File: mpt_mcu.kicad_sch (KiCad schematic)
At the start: 11 parts, among them SW2 KMR421GULCLFS, SW3 KMR421GULCLFS, U4 ESP32-S3-WROOM-1-N4R2

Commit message: Added Info-Table for STAT Pins and LEDS of Charger Work In Progress regulation for Display driving (currently not working)
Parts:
- R20: value 1k -> 100R; symbol db:resistor_0603/00.018.0009.0045 -> db:resistor_0603/00.018.0009.0044; Dist1# 311-1.00KHRCT-ND -> 311-100HRCT-ND; MFR# RC0603FR-071KL -> RC0603FR-07100RL
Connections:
- net +3V3 renamed +3V4
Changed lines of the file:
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@@
 			)
 		)
-		(property "Value" "+3V3"
+		(property "Value" "+3V4"
 			(at 88.9 46.6669 0)
 			(show_name no)
@@
 			)
 		)
-		(property "Value" "+3V3"
+		(property "Value" "+3V4"
 			(at 88.9 74.6069 0)
 			(show_name no)
@@
 			)
 		)
-		(property "Value" "+3V3"
+		(property "Value" "+3V4"
 			(at 209.55 56.8269 0)
 			(show_name no)
@@
 	)
 	(symbol
-		(lib_id "db:resistor_0603/00.018.0009.0045")
+		(lib_id "db:resistor_0603/00.018.0009.0044")
 		(at 209.55 66.04 0)
 		(unit 1)
@@
 			)
 		)
-		(property "Value" "1k"
+		(property "Value" "100R"
 			(at 211.074 67.2521 0)
 			(show_name no)
@@
 			)
 		)
-		(property "Description" "R 1k 0603"
+		(property "Description" "R 100R 0603"
 			(at 209.55 66.04 0)
 			(hide yes)
@@
 			)
 		)
-		(property "MFR#" "RC0603FR-071KL"
+		(property "MFR#" "RC0603FR-07100RL"
 			(at 209.55 66.04 0)
 			(hide yes)
@@
 			)
 		)
-		(property "Dist1#" "311-1.00KHRCT-ND"
+		(property "Dist1#" "311-100HRCT-ND"
 			(at 209.55 66.04 0)
 			(hide yes)
@@
 			)
 		)
-		(property "Value" "+3V3"
+		(property "Value" "+3V4"
 			(at 136.652 75.946 0)
 			(show_name no)

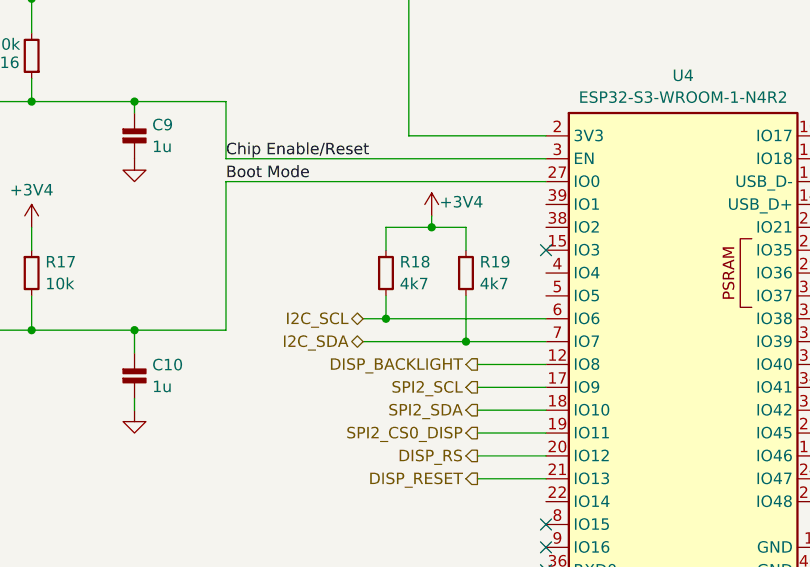
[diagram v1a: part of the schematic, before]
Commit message: Changed LED Driver for one with lower Headroom
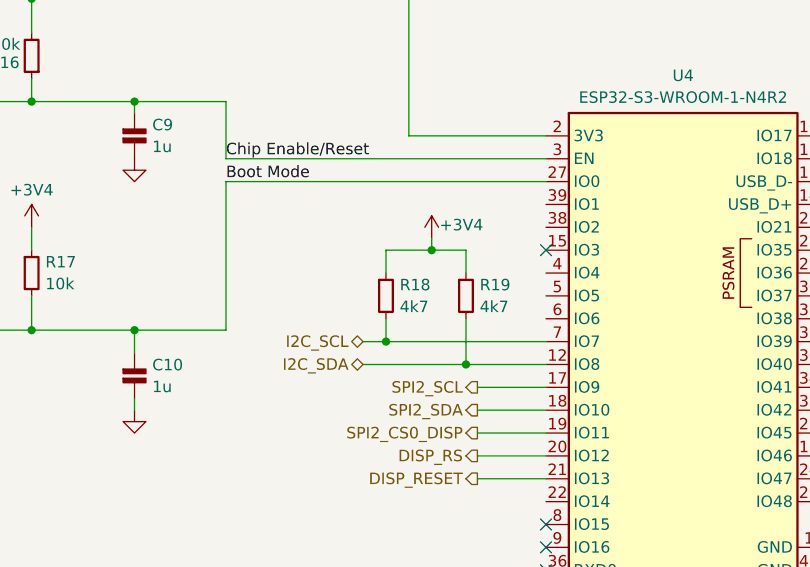
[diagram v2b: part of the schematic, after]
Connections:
- net DISP_BACKLIGHT is gone; now on net I2C_SDA: U4.12 (IO8)
- net I2C_SCL: now also U4.7 (IO7); no longer U4.6 (IO6)
- net I2C_SDA: no longer U4.7 (IO7)
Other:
- moved on the sheet: R18, R19

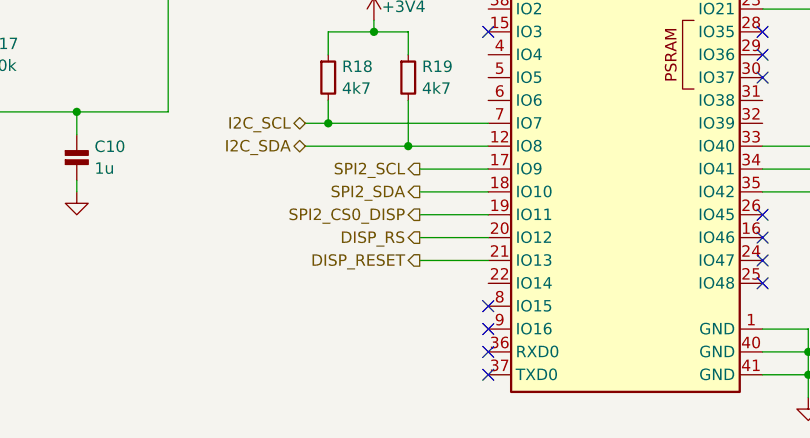
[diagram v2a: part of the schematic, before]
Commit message: RTC Finished, changes to User Buttons
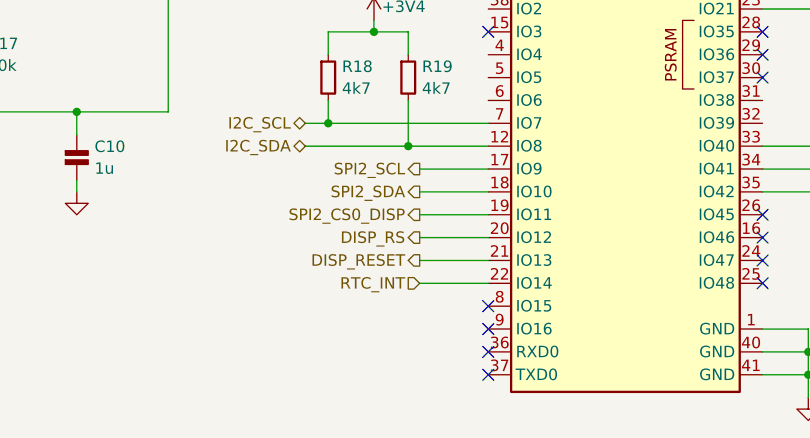
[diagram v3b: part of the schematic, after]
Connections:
- net RTC_INT: now reaches U4.22 (IO14)
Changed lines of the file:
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@@
+	(wire
+		(pts
+			(xy 138.43 109.22) (xy 146.05 109.22)
+		)
+		(stroke
+			(width 0)
+			(type default)
+		)
+	)
 	(wire
 		(pts
@@
 		(effects
 			(font
+				(size 1.27 1.27)
+			)
+			(justify right)
+		)
+	)
+	(hierarchical_label "RTC_INT"
+		(shape input)
+		(at 138.43 109.22 180)
+		(effects
+			(font

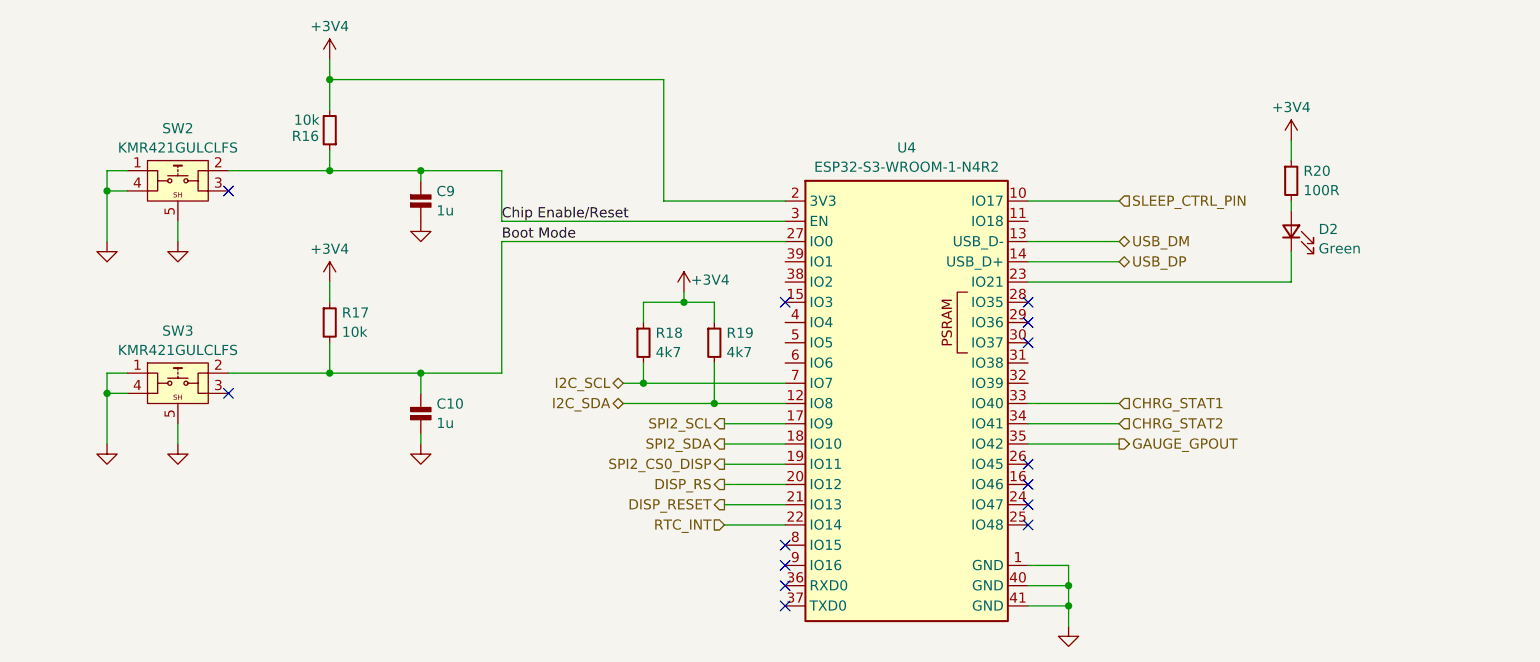
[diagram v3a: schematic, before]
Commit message: Updated PCB Layout with new Buck Boost, Display driver and STAT Led logic
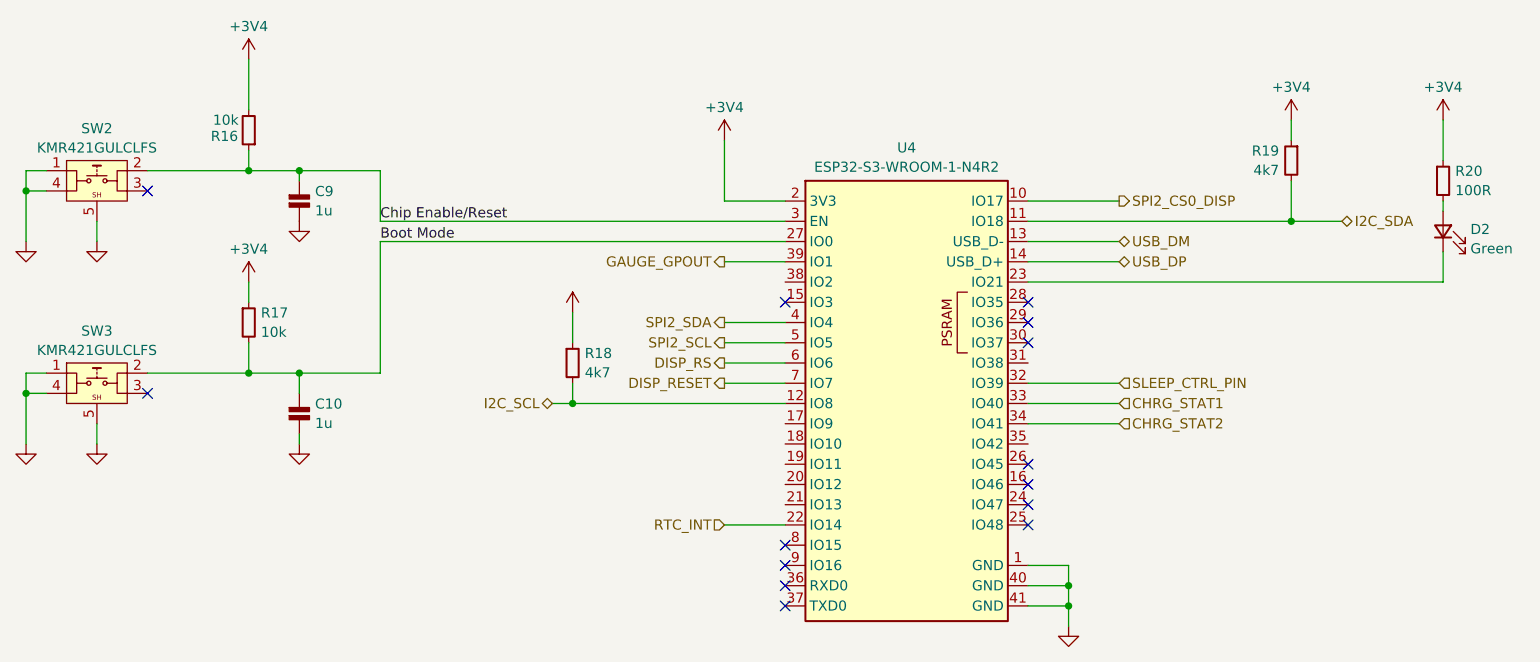
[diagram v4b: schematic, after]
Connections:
- net DISP_RESET: now also U4.7 (IO7); no longer U4.21 (IO13)
- net DISP_RS: now also U4.6 (IO6); no longer U4.20 (IO12)
- net GAUGE_GPOUT: now also U4.39 (IO1); no longer U4.35 (IO42)
- net I2C_SCL: now also U4.12 (IO8); no longer U4.7 (IO7)
- net I2C_SDA: now also U4.11 (IO18); no longer U4.12 (IO8)
- net SLEEP_CTRL_PIN: now also U4.32 (IO39); no longer U4.10 (IO17)
- net SPI2_CS0_DISP: now also U4.10 (IO17); no longer U4.19 (IO11)
- net SPI2_SCL: now also U4.5 (IO5); no longer U4.17 (IO9)
- net SPI2_SDA: now also U4.4 (IO4); no longer U4.18 (IO10)
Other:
- moved on the sheet: C10, C9, D2, R16, R17, R20, SW2, SW3

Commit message: Sleep Control Sub-Sheet created, Hirarchy Labels renamed connected
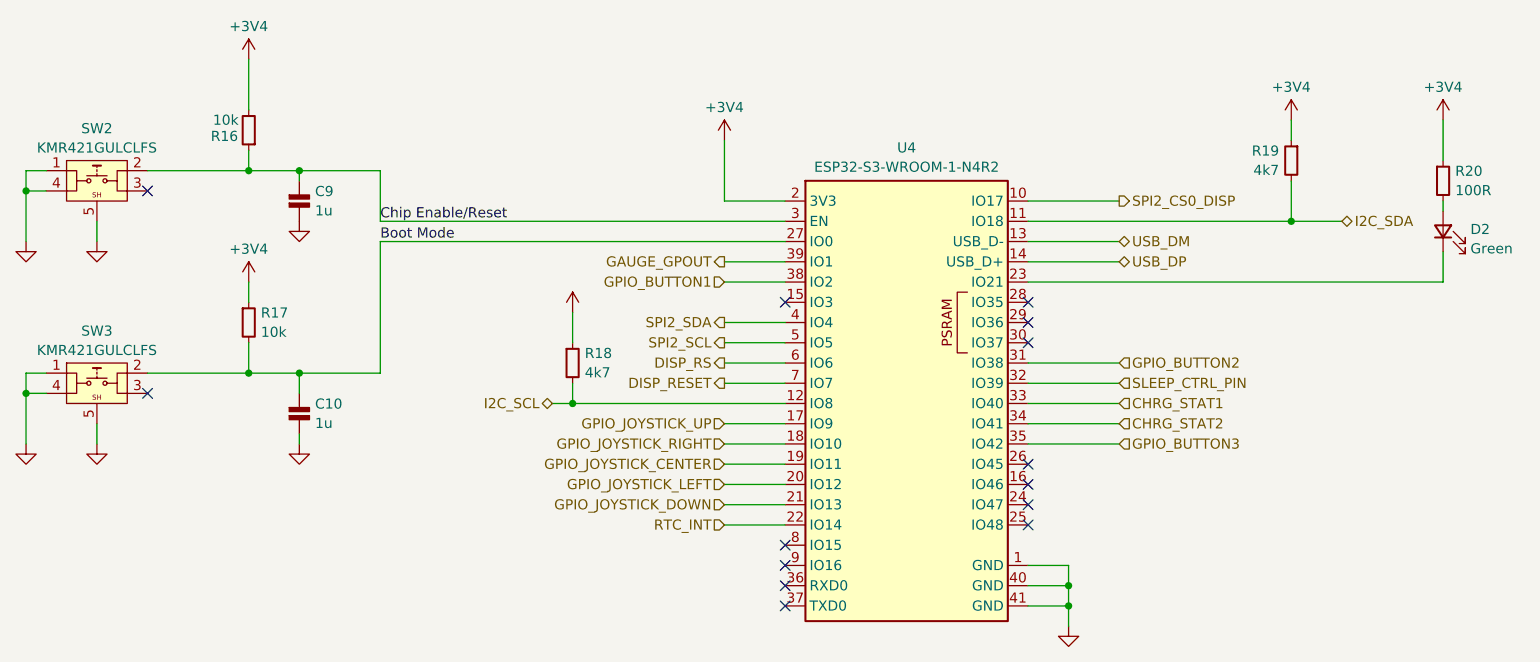
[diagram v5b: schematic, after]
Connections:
- net GPIO_JOYSTICK_UP: now reaches U4.17 (IO9)
- net GPIO_JOYSTICK_RIGHT: now reaches U4.18 (IO10)
- net GPIO_JOYSTICK_CENTER: now reaches U4.19 (IO11)
- net GPIO_JOYSTICK_LEFT: now reaches U4.20 (IO12)
- net GPIO_JOYSTICK_DOWN: now reaches U4.21 (IO13)
- net GPIO_BUTTON2: now reaches U4.31 (IO38)
- net GPIO_BUTTON3: now reaches U4.35 (IO42)
- net GPIO_BUTTON1: now reaches U4.38 (IO2)
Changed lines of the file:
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@@
+	(wire
+		(pts
+			(xy 187.96 88.9) (xy 176.53 88.9)
+		)
+		(stroke
+			(width 0)
+			(type default)
+		)
+	)
 	(wire
 		(pts
@@
 	(wire
 		(pts
+			(xy 138.43 99.06) (xy 146.05 99.06)
+		)
+		(stroke
+			(width 0)
+			(type default)
+		)
+	)
+	(wire
+		(pts
 			(xy 85.09 66.04) (xy 85.09 64.77)
 		)
@@
 	(wire
 		(pts
+			(xy 187.96 99.06) (xy 176.53 99.06)
+		)
+		(stroke
+			(width 0)
+			(type default)
+		)
+	)
+	(wire
+		(pts
 			(xy 78.74 78.74) (xy 78.74 81.28)
 		)
@@
 	(wire
 		(pts
+			(xy 138.43 104.14) (xy 146.05 104.14)
+		)
+		(stroke
+			(width 0)
+			(type default)
+		)
+	)
+	(wire
+		(pts
 			(xy 176.53 119.38) (xy 181.61 119.38)
 		)
@@
 	(wire
 		(pts
+			(xy 138.43 106.68) (xy 146.05 106.68)
+		)
+		(stroke
+			(width 0)
+			(type default)
+		)
+	)
+	(wire
+		(pts
 			(xy 146.05 76.2) (xy 138.43 76.2)
 		)
@@
 	(wire
 		(pts
+			(xy 138.43 96.52) (xy 146.05 96.52)
+		)
+		(stroke
+			(width 0)
+			(type default)
+		)
+	)
+	(wire
+		(pts
 			(xy 176.53 71.12) (xy 215.9 71.12)
 		)
@@
 		(pts
 			(xy 116.84 93.98) (xy 119.38 93.98)
+		)
+		(stroke
+			(width 0)
+			(type default)
+		)
+	)
+	(wire
+		(pts
+			(xy 138.43 78.74) (xy 146.05 78.74)
+		)
+		(stroke
+			(width 0)
+			(type default)
+		)
+	)
+	(wire
+		(pts
+			(xy 138.43 101.6) (xy 146.05 101.6)
 		)
 		(stroke
@@
 			)
 			(justify left bottom)
+		)
+	)
+	(hierarchical_label "GPIO_JOYSTICK_DOWN"
+		(shape input)
+		(at 138.43 106.68 180)
+		(effects
+			(font
+				(size 1.27 1.27)
+			)
+			(justify right)
+		)
+	)
+	(hierarchical_label "GPIO_JOYSTICK_CENTER"
+		(shape input)
+		(at 138.43 101.6 180)
+		(effects
+			(font
+				(size 1.27 1.27)
+			)
+			(justify right)
+		)
+	)
+	(hierarchical_label "GPIO_BUTTON3"
+		(shape input)
+		(at 187.96 99.06 0)
+		(effects
+			(font
+				(size 1.27 1.27)
+			)
+			(justify left)
 		)
 	)
@@
 		)
 	)
+	(hierarchical_label "GPIO_JOYSTICK_RIGHT"
+		(shape input)
+		(at 138.43 99.06 180)
+		(effects
+			(font
+				(size 1.27 1.27)
+			)
+			(justify right)
+		)
+	)
+	(hierarchical_label "GPIO_JOYSTICK_UP"
+		(shape input)
+		(at 138.43 96.52 180)
+		(effects
+			(font
+				(size 1.27 1.27)
+			)
+			(justify right)
+		)
+	)
 	(hierarchical_label "I2C_SCL"
 		(shape bidirectional)
@@
 		)
 	)
+	(hierarchical_label "GPIO_BUTTON2"
+		(shape input)
+		(at 187.96 88.9 0)
+		(effects
+			(font
+				(size 1.27 1.27)
+			)
+			(justify left)
+		)
+	)
 	(hierarchical_label "RTC_INT"
 		(shape input)
@@
 			)
 			(justify left)
+		)
+	)
+	(hierarchical_label "GPIO_JOYSTICK_LEFT"
+		(shape input)
+		(at 138.43 104.14 180)
+		(effects
+			(font
+				(size 1.27 1.27)
+			)
+			(justify right)
 		)
 	)
@@
 		(effects
 			(font
+				(size 1.27 1.27)
+			)
+			(justify right)
+		)
+	)
+	(hierarchical_label "GPIO_BUTTON1"
+		(shape input)
+		(at 138.43 78.74 180)
+		(effects
+			(font

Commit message: Make Block Titles consistent in size Remove not connected marks on mcu for pins which can be used for user buttons and other stuff Add User button hierarchy lables for Button 4 & 5 on MCU sheet Fix hierarchichal pin names on the block not matching the sheet
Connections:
- net GPIO_BUTTON4: now reaches U4.24 (IO47)
- net GPIO_BUTTON5: now reaches U4.25 (IO48)
- no-connect marks 14 -> 10
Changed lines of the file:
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@@
 		(title "M.P.T MCU")
 		(company "Hochschule Luzern, Technik & Architektur")
+		(comment 1 "Designed by Nico Theiler & Dominik Grob")
 	)
 	(junction
@@
 	)
 	(no_connect
-		(at 176.53 106.68)
-	)
-	(no_connect
 		(at 66.04 67.31)
 	)
@@
 	)
 	(no_connect
-		(at 146.05 111.76)
-	)
-	(no_connect
 		(at 146.05 81.28)
 	)
@@
 	)
 	(no_connect
-		(at 176.53 109.22)
-	)
-	(no_connect
 		(at 146.05 116.84)
 	)
@@
 		(at 146.05 119.38)
 	)
-	(no_connect
-		(at 146.05 114.3)
-	)
 	(wire
 		(pts
@@
 	(wire
 		(pts
+			(xy 176.53 106.68) (xy 187.96 106.68)
+		)
+		(stroke
+			(width 0)
+			(type default)
+		)
+	)
+	(wire
+		(pts
 			(xy 176.53 91.44) (xy 187.96 91.44)
 		)
@@
 		(pts
 			(xy 50.8 99.06) (xy 50.8 92.71)
+		)
+		(stroke
+			(width 0)
+			(type default)
+		)
+	)
+	(wire
+		(pts
+			(xy 176.53 109.22) (xy 187.96 109.22)
 		)
 		(stroke
@@
 			)
 			(justify left bottom)
+		)
+	)
+	(hierarchical_label "GPIO_BUTTON5"
+		(shape input)
+		(at 187.96 109.22 0)
+		(effects
+			(font
+				(size 1.27 1.27)
+			)
+			(justify left)
 		)
 	)
@@
 		)
 	)
+	(hierarchical_label "GPIO_BUTTON4"
+		(shape input)
+		(at 187.96 106.68 0)
+		(effects
+			(font
+				(size 1.27 1.27)
+			)
+			(justify left)
+		)
+	)

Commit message: Footprints added, Userbuttons and RTC added on PCB Layout
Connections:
- net GPIO_BUTTON5: no longer names the net of U4.25 (IO48)
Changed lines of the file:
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@@
-	(wire
-		(pts
-			(xy 176.53 109.22) (xy 187.96 109.22)
-		)
-		(stroke
-			(width 0)
-			(type default)
-		)
-	)
 	(wire
 		(pts
@@
 		)
 	)
-	(hierarchical_label "GPIO_BUTTON5"
-		(shape input)
-		(at 187.96 109.22 0)
-		(effects
-			(font
-				(size 1.27 1.27)
-			)
-			(justify left)
-		)
-	)

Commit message: Started routing of componentes
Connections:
- net CHRG_STAT1: now also U4.34 (IO41); no longer U4.33 (IO40)
- net CHRG_STAT2: now also U4.35 (IO42); no longer U4.34 (IO41)
- net GPIO_BUTTON3: now also U4.32 (IO39); no longer U4.35 (IO42)
- net GPIO_BUTTON4: now also U4.33 (IO40); no longer U4.24 (IO47)
- net I2C_SCL: now also U4.10 (IO17); no longer U4.12 (IO8)
- net I2C_SDA: now also U4.9 (IO16); no longer U4.11 (IO18)
- net SLEEP_CTRL_PIN: now also U4.24 (IO47); no longer U4.32 (IO39)
- net SPI2_CS0_DISP: now also U4.8 (IO15); no longer U4.10 (IO17)
